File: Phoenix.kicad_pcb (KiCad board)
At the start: 2 copper layers, 52 parts, among them J1 Mini USB Female, J2 Battery Connector, J3 Pyro Connectors, Q1 IRFML8244TRPBF, Q2 IRFML8244TRPBF, Q3 IRFML8244TRPBF, Q4 IRFML8244TRPBF, U1 RP2040, U3 AMS1117-3.3, U6 ADXL343, Y1 12MHz

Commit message: Other changes I cant remember
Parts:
- added RN1: 22k, Resistor_SMD:R_Array_Convex_4x1206, F.Cu at (155.2, -17.8)
- added RN2: 22k, Resistor_SMD:R_Array_Convex_4x1206, F.Cu at (185.4, -16.6)
- added RN3: 22k, Resistor_SMD:R_Array_Convex_4x1206, F.Cu at (170.4, -6.69)
- added RN4: 22k, Resistor_SMD:R_Array_Convex_4x1206, F.Cu at (185.4, -6.69)
- D4, D5, D6, D7: value 3v3, MMSZ4684T1G -> 1N4007
- moved D4 114.2 mm to (160.3, -19.8), turned to 180 degrees
- moved D6 92.8 mm to (193.8, -8.55)
- moved D7 90.3 mm to (203.8, -8.55)
- moved D5 87.7 mm to (203.8, -15.5)
- moved Q1 79.6 mm to (160.3, -16.5), turned to 180 degrees
- moved U3 14.5 mm to (81.2, 55.5)
- moved AE2 1.48 mm to (128.3, -22.1)
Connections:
- D4 pad 1: /GPIO & Pyro/Cont1 -> +3V3
- D4 pad 2: GND -> /GPIO & Pyro/Cont1
- D5 pad 1: /GPIO & Pyro/Cont2 -> +3V3
- D5 pad 2: GND -> /GPIO & Pyro/Cont2
- D6 pad 1: /GPIO & Pyro/Cont3 -> +3V3
- D6 pad 2: GND -> /GPIO & Pyro/Cont3
- D7 pad 1: /GPIO & Pyro/Cont4 -> +3V3
- D7 pad 2: GND -> /GPIO & Pyro/Cont4

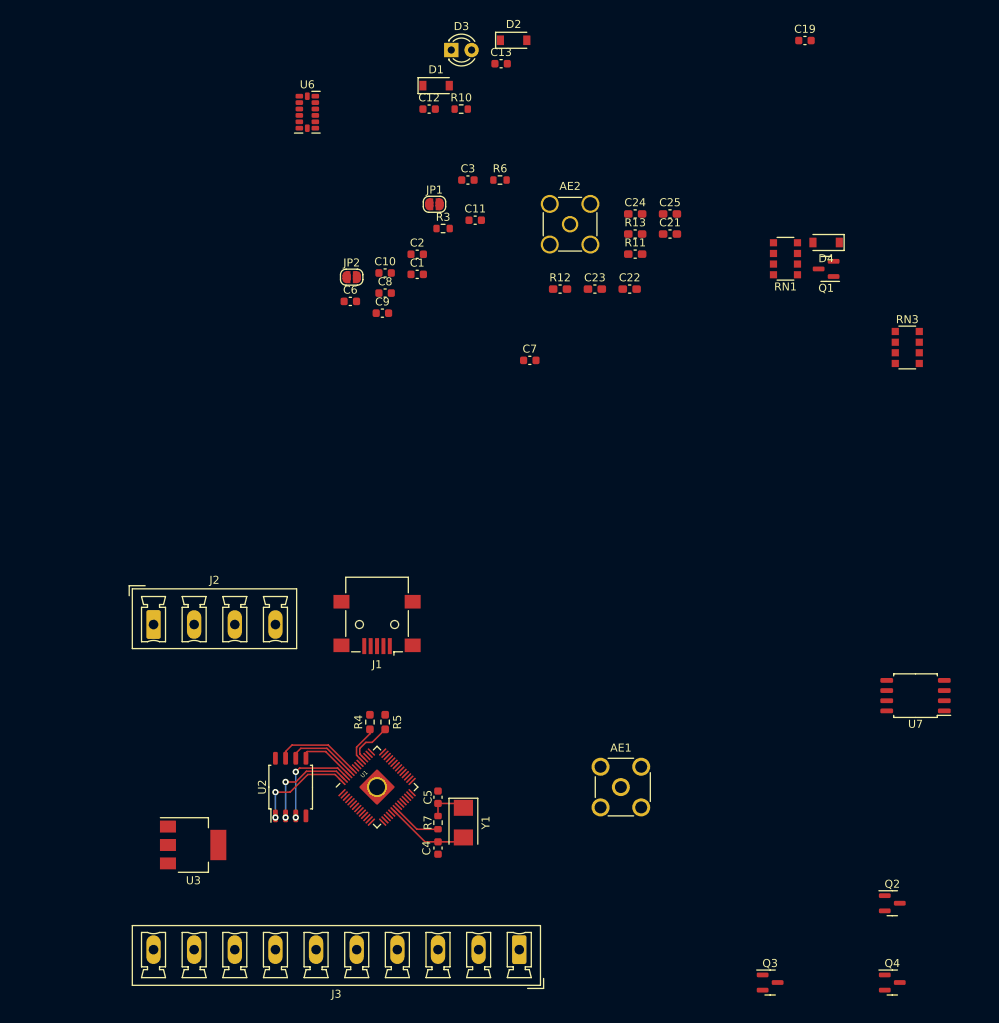
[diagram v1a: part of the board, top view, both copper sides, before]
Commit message: Connected the sensors, flash chip, Need to connect the radio and GPS
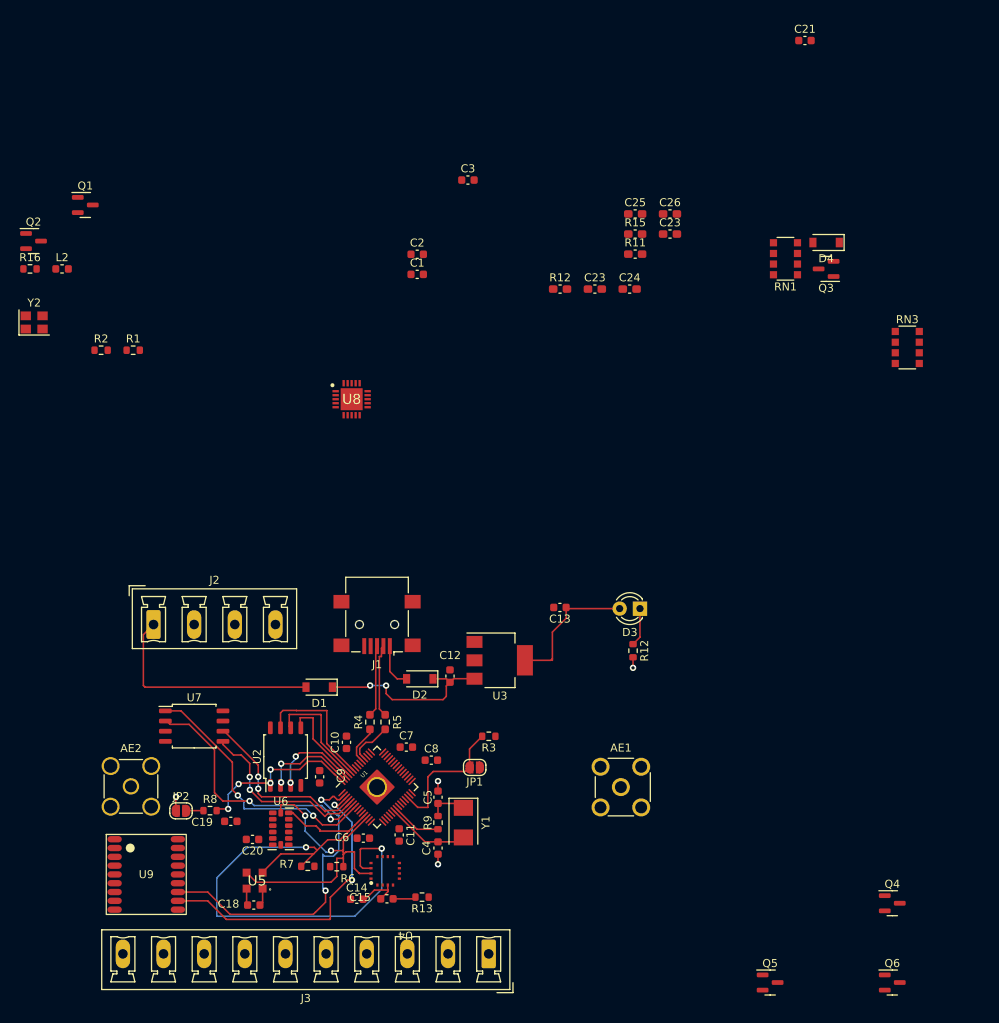
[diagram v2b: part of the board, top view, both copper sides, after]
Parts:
- added C14: 470n, Capacitor_SMD:C_0603_1608Metric, F.Cu at (101.6, 62.3)
- added C15: 10n, Capacitor_SMD:C_0603_1608Metric, F.Cu at (105.4, 62.2)
- added C18: 100nF, Capacitor_SMD:C_0603_1608Metric, F.Cu at (88.7, 63.0)
- added C19: 100nF, Capacitor_SMD:C_0603_1608Metric, F.Cu at (85.9, 52.5)
- added C20: 100nF, Capacitor_SMD:C_0603_1608Metric, F.Cu at (88.6, 54.8)
- added L2: 47n, Inductor_SMD:L_0603_1608Metric, F.Cu at (64.8, -16.5)
- added Q1: 2N7000, Package_TO_SOT_SMD:SOT-23, F.Cu at (67.7, -24.5)
- added Q2: BSS84, Package_TO_SOT_SMD:SOT-23, F.Cu at (61.2, -20.0)
- added R1: 10k, Resistor_SMD:R_0603_1608Metric, F.Cu at (73.7, -6.35)
- added R13: 10k, Resistor_SMD:R_0603_1608Metric, F.Cu at (109.8, 62.0)
- added R16: 10, Resistor_SMD:R_0603_1608Metric, F.Cu at (60.8, -16.5)
- added R2: 10k, Resistor_SMD:R_0603_1608Metric, F.Cu at (69.7, -6.35)
- added R6: 10k, Resistor_SMD:R_0603_1608Metric, F.Cu at (99.1, 58.2)
- added R7: 10k, Resistor_SMD:R_0603_1608Metric, F.Cu at (95.5, 58.2)
- added U4: I3G4250D, YAR_Sensors:I3G4250D, F.Cu at (105.2, 58.7)
- added U5: MS5637-02BA03, YAR_Sensors:MS5637_1, F.Cu at (88.8, 60.0)
- added U8: Si4468/7, YAR_RF:SI4468-A2A-IMR, F.Cu at (101.0, -0.22)
- added U9: L70B-M39, YAR_GPS:L70R, F.Cu at (75.3, 59.2)
- added Y2: 30MHz, Oscillator:Oscillator_SMD_Abracon_ASE-4Pin_3.2x2.5mm, F.Cu at (61.3, -9.82)
- moved U7 90.3 mm to (81.3, 40.6), turned to 0 degrees
- moved U6 89.6 mm to (92.1, 53.5)
- moved AE2 89.2 mm to (73.4, 48.2)
- moved R8 86.8 mm to (83.3, 51.2)
- moved D2 80.7 mm to (109.5, 34.7), turned to 180 degrees
- moved C11 77.4 mm to (106.9, 54.2), turned to -90 degrees
- moved D1 76.6 mm to (96.9, 35.8), turned to 180 degrees
- moved D3 73.7 mm to (137.0, 26.0), turned to 180 degrees
- moved R12 71.0 mm to (136.1, 31.2), turned to -90 degrees
- moved C12 70.9 mm to (113.3, 34.4), turned to 90 degrees
- moved JP1 70.6 mm to (116.3, 45.8), turned to 180 degrees
- moved JP2 70.0 mm to (79.6, 51.2)
- moved C13 68.4 mm to (127.0, 25.8), turned to 180 degrees
- moved C6 67.1 mm to (102.4, 54.6)
- moved R3 63.7 mm to (118.1, 41.9), turned to 180 degrees
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- renumbered C19 to C21, C21 to C23, C22 to C24, C24 to C25, C25 to C26, Q1 to Q3, Q2 to Q4, Q3 to Q5, Q4 to Q6, R10 to R12, R13 to R15, R6 to R8, R7 to R9
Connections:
- U1 pad 13: /RP2040/Accel1 -> /Accelerometer/Accel1
- U1 pad 14: /RP2040/Accel2 -> /Accelerometer/Accel2
- U1 pad 15: /RP2040/Gyro1 -> /Accelerometer/Gyro1
- U1 pad 16: /RP2040/Gyro2 -> /Accelerometer/Gyro2
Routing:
- net /Accelerometer/SDA: track 0.00 -> 78.9 mm, vias 0 -> 2
- net /Accelerometer/SCL: track 0.00 -> 41.0 mm, vias 0 -> 2
- net /GPS/Tx: track 0.00 -> 39.6 mm, vias 0 -> 2
- net /GPS/Rx: track 0.00 -> 38.6 mm, vias 0 -> 2
- net /Flash Storage/CS0: track 0.00 -> 33.1 mm, vias 0 -> 2
- net /Flash Storage/Rx: track 0.00 -> 32.7 mm, vias 0 -> 2
- net +BATT: track 0.00 -> 28.6 mm
- net Net-(C12-Pad1): track 0.00 -> 23.3 mm, vias 0 -> 2
- net /Flash Storage/Tx: track 0.00 -> 23.1 mm, vias 0 -> 2
- net /Flash Storage/SCK: track 0.00 -> 22.8 mm, vias 0 -> 2
- net +3V3: track 0.00 -> 17.6 mm
- net Net-(JP1-Pad2): track 0.00 -> 17.1 mm
- net /Power Supply/D-: track 0.00 -> 9.25 mm
- net /Power Supply/D+: track 0.00 -> 8.95 mm
- net QSPI_SS: track 12.8 -> 21.4 mm, vias 2 -> 4
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
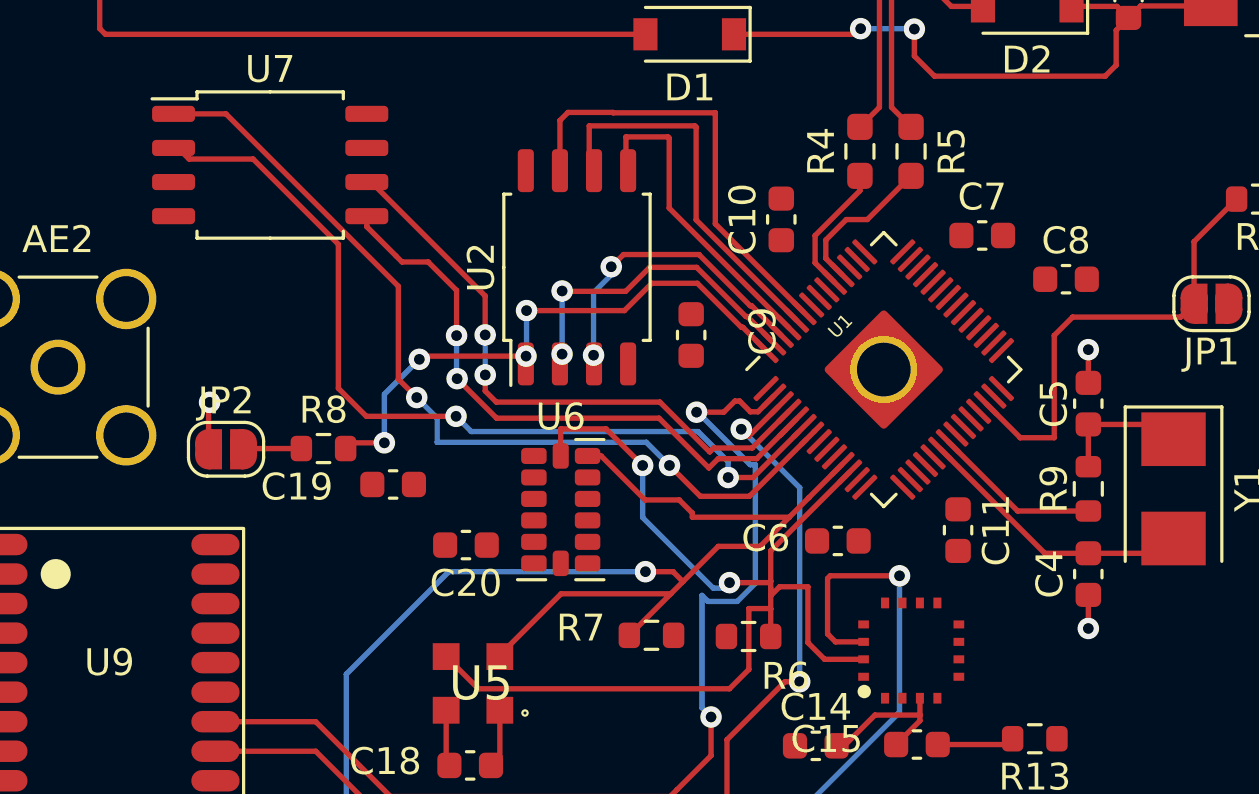
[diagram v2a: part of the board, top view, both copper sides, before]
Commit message: Rearranged IO pins to make routing easier. Removed reset, changed BOOTSEL to button
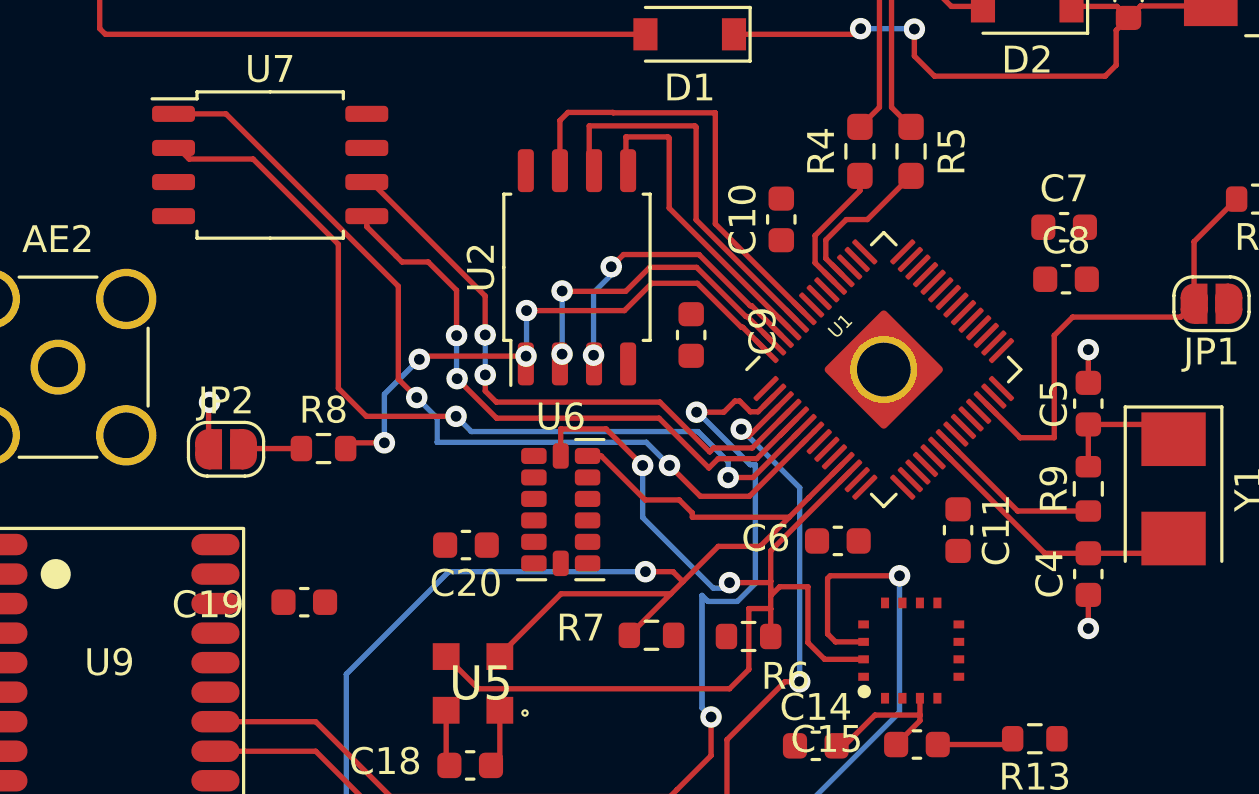
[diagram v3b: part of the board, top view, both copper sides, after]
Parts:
- moved C19 5.50 mm to (82.5, 56.9)
- moved C7 3.07 mm to (110.9, 43.0)
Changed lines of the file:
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@@
   )
   (footprint "Capacitor_SMD:C_0603_1608Metric" (layer "F.Cu")
-    (at 107.806685 43.265551)
+    (at 110.858 42.9575)
     (descr "Capacitor SMD 0603 (1608 Metric), square (rectangular) end terminal, IPC_7351 nominal, (Body size source: IPC-SM-782 page 76, https://www.pcb-3d.com/wordpress/wp-content/uploads/ipc-sm-782a_amendment_1_and_2.pdf), generated with kicad-footprint-generator")
     (tags "capacitor")
@@
   )
   (footprint "Capacitor_SMD:C_0603_1608Metric" (layer "F.Cu")
-    (at 85.860789 52.541689 180)
+    (at 82.55 56.9275 180)
     (descr "Capacitor SMD 0603 (1608 Metric), square (rectangular) end terminal, IPC_7351 nominal, (Body size source: IPC-SM-782 page 76, https://www.pcb-3d.com/wordpress/wp-content/uploads/ipc-sm-782a_amendment_1_and_2.pdf), generated with kicad-footprint-generator")
     (tags "capacitor")
@@
     )
   )
-  (gr_rect (start 68.58 73.66) (end 139.7 22.86) (layer "Dwgs.User") (width 0.15) (fill none))
+  (gr_rect (start 67.818 73.66) (end 139.7 22.86) (layer "Dwgs.User") (width 0.15) (fill none))
   (gr_line (start 68.58 48.26) (end 139.7 48.26) (layer "Dwgs.User") (width 0.15))
   (dimension (type aligned) (layer "Dwgs.User")

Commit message: Rearrange parts of PCB
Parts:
- removed the C23 at (131.4, -14.0)
- removed JP1: RESET, Jumper:SolderJumper-2_P1.3mm_Open_RoundedPad1.0x1.5mm
- removed the R12 at (127.0, -14.0)
- removed R3: 1k, Resistor_SMD:R_0603_1608Metric
- removed R6, R7: 10k, Resistor_SMD:R_0603_1608Metric
- added C16: 10uF, Capacitor_SMD:C_0603_1608Metric, F.Cu at (128.3, 43.1)
- added C17: 100nF, Capacitor_SMD:C_0603_1608Metric, F.Cu at (179.3, 100.4)
- added C22: 5.1p, Capacitor_SMD:C_0603_1608Metric, F.Cu at (123.5, 59.1)
- added CM1: 6.8n, Capacitor_SMD:C_0603_1608Metric, F.Cu at (127.3, 61.4)
- added CM2: 3.3p, Capacitor_SMD:C_0603_1608Metric, F.Cu at (131.8, 59.9)
- added CM3: 3.3p, Capacitor_SMD:C_0603_1608Metric, F.Cu at (136.4, 59.8)
- added CR1: 3p, Capacitor_SMD:C_0603_1608Metric, F.Cu at (124.2, 64.4)
- added CR2: 1.2p, Capacitor_SMD:C_0603_1608Metric, F.Cu at (125.0, 62.1)
- added L1: 3.3n, Inductor_SMD:L_0603_1608Metric, F.Cu at (126.5, 59.1)
- added LM1: 12n, Inductor_SMD:L_0603_1608Metric, F.Cu at (129.5, 59.1)
- added LM2: 24n, Inductor_SMD:L_0603_1608Metric, F.Cu at (134.1, 59.1)
- added LM3: 12n, Inductor_SMD:L_0603_1608Metric, F.Cu at (138.7, 59.1)
- added LR1: 18n, Inductor_SMD:L_0603_1608Metric, F.Cu at (122.7, 61.4)
- added LR2: 24n, Inductor_SMD:L_0603_1608Metric, F.Cu at (125.0, 60.6)
- added Lc1: 120n, Inductor_SMD:L_0603_1608Metric, F.Cu at (122.7, 56.8)
- added R10: 33k, Resistor_SMD:R_0603_1608Metric, F.Cu at (179.3, 92.6)
- added R14: 10k, Resistor_SMD:R_0603_1608Metric, F.Cu at (65.1, 60.4)
- J2: footprint Connector_Phoenix_MC_HighVoltage:PhoenixContact_MCV_1,5_4-G-5.08_1x04_P5.08mm_Vertical -> YAR_Connectors:ScrewTerm_2.54x04
- J3: footprint Connector_Phoenix_MC_HighVoltage:PhoenixContact_MCV_1,5_10-G-5.08_1x10_P5.08mm_Vertical -> YAR_Connectors:ScrewTerm_2.54x10
- JP2: footprint Jumper:SolderJumper-2_P1.3mm_Open_RoundedPad1.0x1.5mm -> Button_Switch_SMD:SW_SPST_B3U-1000P
- R11: value 100R -> 12k; footprint Capacitor_SMD:C_0603_1608Metric_Pad1.08x0.95mm_HandSolder -> Resistor_SMD:R_0603_1608Metric
- moved C2 294.3 mm to (-143.8, 132.0)
- moved C3 294.3 mm to (-137.5, 122.7)
- moved D4 294.3 mm to (-92.7, 130.5)
- moved D5 294.3 mm to (-49.1, 134.9)
- moved D6 294.3 mm to (-59.2, 141.8)
- moved D7 294.3 mm to (-49.1, 141.8)
- moved Q3 294.3 mm to (-92.7, 133.8)
- moved RN1 294.3 mm to (-97.8, 132.6)
- moved RN2 294.3 mm to (-67.6, 133.8)
- moved RN3 294.3 mm to (-82.5, 143.7)
- moved RN4 294.3 mm to (-67.6, 143.7)
- moved C1 227.6 mm to (-75.7, 117.0), turned to -90 degrees
- moved R11 120.5 mm to (183.3, 92.6)
- moved C21 117.2 mm to (101.6, 57.8), turned to -90 degrees
- moved C25 105.2 mm to (65.7, 54.5)
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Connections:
- R1 pad 1: /I2C0.SDA -> /Accelerometer/SDA
- R11 pad 1: Net-(R11-Pad1) -> /Power Supply/VBat/4
- R11 pad 2: Net-(R11-Pad2) -> GND
- R2 pad 1: /I2C0.SCL -> /Accelerometer/SCL
- U1 pad 11: /Accelerometer/SDA -> unconnected-(U1-Pad11)
- U1 pad 12: /Accelerometer/SCL -> unconnected-(U1-Pad12)
- U1 pad 13: /Accelerometer/Accel1 -> unconnected-(U1-Pad13)
- U1 pad 14: /Accelerometer/Accel2 -> /Flash Storage/CS0
- U1 pad 15: /Accelerometer/Gyro1 -> /Flash Storage/Rx
- U1 pad 16: /Accelerometer/Gyro2 -> /Flash Storage/CS1
- U1 pad 17: /GPIO & Pyro/Pyro1 -> /Flash Storage/SCK
- U1 pad 18: /GPIO & Pyro/Pyro2 -> /Flash Storage/Tx
- U1 pad 26: Net-(JP1-Pad2) -> +3V3
- U1 pad 27: /GPIO & Pyro/Pyro3 -> unconnected-(U1-Pad27)
- U1 pad 28: /GPIO & Pyro/Pyro4 -> unconnected-(U1-Pad28)
- U1 pad 29: /GPIO & Pyro/Cont1 -> /Accelerometer/Radio
- U1 pad 30: /GPIO & Pyro/Cont2 -> unconnected-(U1-Pad30)
- U1 pad 31: /GPIO & Pyro/Cont3 -> /Accelerometer/SDA
- U1 pad 32: /GPIO & Pyro/Cont4 -> /Accelerometer/SCL
- U1 pad 34: /GPIO & Pyro/GPIO22 -> /Accelerometer/Accel2
- U1 pad 35: /GPIO & Pyro/GPIO23 -> /Accelerometer/Accel1
- U1 pad 36: /GPIO & Pyro/GPIO24 -> /Accelerometer/Gyro2
- U1 pad 37: /GPIO & Pyro/GPIO25 -> /Accelerometer/Gyro1
- U1 pad 38: /GPIO & Pyro/ADC0 -> unconnected-(U1-Pad38)
- U1 pad 39: /GPIO & Pyro/ADC1 -> unconnected-(U1-Pad39)
- U1 pad 4: /Flash Storage/SCK -> unconnected-(U1-Pad4)
- U1 pad 40: /GPIO & Pyro/ADC2 -> unconnected-(U1-Pad40)
- U1 pad 5: /Flash Storage/Tx -> unconnected-(U1-Pad5)
- U1 pad 6: /Flash Storage/Rx -> unconnected-(U1-Pad6)
- U1 pad 7: /Flash Storage/CS0 -> unconnected-(U1-Pad7)
- U1 pad 8: /Flash Storage/CS1 -> unconnected-(U1-Pad8)
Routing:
- net /Accelerometer/SDA: track 78.9 -> 33.6 mm, vias 2 -> 6
- net /GPS/Tx: track 39.6 -> 0.00 mm, vias 2 -> 0
- net /GPS/Rx: track 38.6 -> 0.00 mm, vias 2 -> 0
- net /Accelerometer/Radio: track 0.00 -> 20.7 mm
- net Net-(AE2-Pad1): track 0.00 -> 19.1 mm
- net /Flash Storage/CS0: track 33.1 -> 14.1 mm, vias 2 -> 0
- net /Flash Storage/CS1: track 0.00 -> 18.5 mm, vias 0 -> 2
- net /Accelerometer/Gyro1: track 0.00 -> 18.0 mm
- net /Accelerometer/Gyro2: track 0.00 -> 17.8 mm
- net Net-(JP1-Pad2): track 17.1 -> 0.00 mm
- net Net-(Q2-Pad2): track 0.00 -> 13.2 mm
- net /Accelerometer/Accel2: track 0.00 -> 9.05 mm
- net /Accelerometer/Accel1: track 0.00 -> 8.55 mm
- net /Flash Storage/Rx: track 32.7 -> 24.2 mm
- net Net-(C25-Pad1): track 0.00 -> 8.41 mm
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
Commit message: Routed pyros. Placed decoupling capacitors
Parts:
- moved C3 260.4 mm to (109.3, 39.6), turned to 90 degrees
- moved C2 260.3 mm to (99.8, 40.2), turned to 180 degrees
- moved C1 195.4 mm to (104.6, 41.7), turned to 0 degrees
- moved RN3 193.9 mm to (91.4, 58.0), turned to 180 degrees
- moved RN1 191.7 mm to (78.9, 58.2)
- moved D4 181.9 mm to (73.2, 56.0), turned to 0 degrees
- moved Q3 180.9 mm to (72.6, 60.1)
- moved RN4 174.7 mm to (89.9, 68.0), turned to 180 degrees
- moved D6 168.0 mm to (85.3, 56.0)
- moved D7 154.1 mm to (84.8, 65.5)
- moved RN2 153.3 mm to (65.4, 57.6), turned to 180 degrees
- moved D5 134.5 mm to (59.1, 55.0)
- moved R11 134.2 mm to (66.9, 25.9), turned to 90 degrees
- moved R10 124.1 mm to (70.3, 33.3), turned to 90 degrees
- moved Q4 109.3 mm to (59.3, 58.2), turned to 180 degrees
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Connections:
- U1 pad 11: unconnected-(U1-Pad11) -> /GPIO & Pyro/Cont3
- U1 pad 12: unconnected-(U1-Pad12) -> /GPIO & Pyro/Cont4
- U1 pad 4: unconnected-(U1-Pad4) -> /GPIO & Pyro/Pyro1
- U1 pad 5: unconnected-(U1-Pad5) -> /GPIO & Pyro/Pyro2
- U1 pad 6: unconnected-(U1-Pad6) -> /GPIO & Pyro/Pyro3
- U1 pad 7: unconnected-(U1-Pad7) -> /GPIO & Pyro/Pyro4
- U1 pad 8: unconnected-(U1-Pad8) -> /GPIO & Pyro/Cont1
- U1 pad 9: unconnected-(U1-Pad9) -> /GPIO & Pyro/Cont2
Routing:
- net /GPIO & Pyro/Pyro2: track 0.00 -> 51.0 mm, vias 0 -> 4
- net /GPIO & Pyro/Cont2: track 0.00 -> 49.3 mm, vias 0 -> 2
- net /GPIO & Pyro/Pyro1: track 0.00 -> 35.8 mm, vias 0 -> 2
- net /GPIO & Pyro/Cont1: track 0.00 -> 34.4 mm, vias 0 -> 2
- net /GPIO & Pyro/Pyro4: track 0.00 -> 33.9 mm, vias 0 -> 2
- net Fire 3: track 0.00 -> 29.8 mm, vias 0 -> 2
- net /GPIO & Pyro/Cont4: track 0.00 -> 28.9 mm
- net /GPS/Rx: track 0.00 -> 28.0 mm
- net /GPS/Tx: track 0.00 -> 27.2 mm
- net Fire 1: track 0.00 -> 26.6 mm, vias 0 -> 2
- net Fire 2: track 0.00 -> 23.5 mm, vias 0 -> 2
- net Fire 4: track 0.00 -> 22.8 mm, vias 0 -> 2
- net /GPIO & Pyro/Pyro3: track 0.00 -> 22.2 mm, vias 0 -> 2
- net /GPIO & Pyro/Cont3: track 0.18 -> 19.3 mm
- net Net-(RN4-Pad4): track 0.00 -> 4.49 mm
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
